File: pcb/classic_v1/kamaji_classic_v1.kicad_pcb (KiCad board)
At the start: 2 copper layers, 100 x 100 mm, 27 parts, among them J1 USB_A, J2 USB_B, J4 ISP, J5 RJ10, J6 RJ10, J7 RJ10, J8 RJ10, J9 RJ10, Q1 BS170, SW1 SW_Push, SW2 SW_Push, SW3 SW_Push, U1 ATmega328P

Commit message: Classic: Finish first pass of routing
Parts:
- added REF**: MountingHole_3.2mm_M3, MountingHole:MountingHole_3.2mm_M3, F.Cu at (146.5, 53.5)
- added REF**: MountingHole_3.2mm_M3, MountingHole:MountingHole_3.2mm_M3, F.Cu at (53.5, 53.5)
- added REF**: MountingHole_3.2mm_M3, MountingHole:MountingHole_3.2mm_M3, F.Cu at (53.5, 146.5)
- added REF**: MountingHole_3.2mm_M3, MountingHole:MountingHole_3.2mm_M3, F.Cu at (146.5, 146.5)
- J5: value RJ10 -> P1
- J6: value RJ10 -> P2
- J7: value RJ10 -> P3
- J8: value RJ10 -> P4
- J9: value RJ10 -> P5
- U1: value ATmega328P -> ATmega328P-P
- moved R1 7.10 mm to (145.5, 75.9)
- moved J4 2.66 mm to (88.5, 136.5)
- moved R2 2.57 mm to (83.4, 121.3)
- moved BZ1 2.00 mm to (113.4, 140.0)
- moved C1 1.38 mm to (101.9, 102.9)
- moved C2 1.38 mm to (99.2, 116.4)
- moved U1 1.38 mm to (117.0, 105.9)
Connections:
- SW3 pad 1: /CBTN2 -> /CBTN3
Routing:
- net VCC: track 0.00 -> 286.6 mm
- net /CBTN3: track 0.00 -> 88.0 mm, vias 0 -> 2
- net /LCD_RS: track 0.00 -> 74.5 mm, vias 0 -> 1
- net /LCD_EN: track 0.00 -> 71.0 mm, vias 0 -> 1
- net /RESET: track 0.00 -> 67.7 mm, vias 0 -> 1
- net /PLED5: track 0.00 -> 67.4 mm
- net /PLED1: track 0.00 -> 64.5 mm, vias 0 -> 1
- net /PBTN1: track 0.00 -> 63.7 mm, vias 0 -> 1
- net /PBTN5: track 0.00 -> 59.5 mm
- net /PLED3: track 0.00 -> 57.6 mm, vias 0 -> 1
- net /PBTN3: track 0.00 -> 56.9 mm, vias 0 -> 1
- net /PBTN4: track 0.00 -> 54.5 mm, vias 0 -> 1
- net /LCD_D2: track 0.00 -> 53.9 mm
- net /LCD_D1: track 0.00 -> 53.9 mm
- net /LCD_D3: track 0.00 -> 53.9 mm
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- added copper zone on B.Cu, net GND
- added copper zone on F.Cu, net GND
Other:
- outline, holes or cut-outs redrawn

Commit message: Final PCB layout tweaks
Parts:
- DS1: value WC1602A -> LCD 1602
- moved R8 12.0 mm to (54.3, 61.0), turned to 0 degrees
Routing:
- net Net-(J9-Pad2): track 10.1 -> 17.0 mm
- net /PLED5: track 67.4 -> 64.1 mm
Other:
- board text added: "Kamaji Classic v1.0 github.com/iley/kamaji"
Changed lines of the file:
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@@
       (viasonmask false)
       (mode 1)
-      (useauxorigin false)
+      (useauxorigin true)
       (hpglpennumber 1)
       (hpglpenspeed 20)
@@
       (plotinvisibletext false)
       (sketchpadsonfab false)
-      (subtractmaskfromsilk false)
+      (subtractmaskfromsilk true)
       (outputformat 1)
       (mirror false)
-      (drillshape 1)
+      (drillshape 0)
       (scaleselection 1)
-      (outputdirectory "")
+      (outputdirectory "gerbers/")
     )
   )
@@
         (effects (font (size 1 1) (thickness 0.15)))
     )
-    (fp_text value "Contrast" (at -4.96 -2.54 -180) (layer "F.SilkS")
+    (fp_text value "Contrast" (at 5.04 -2.54 -180) (layer "F.SilkS")
         (effects (font (size 1 1) (thickness 0.15)))
     )
@@
     (fp_line (start 13.28 15.26) (end 4.38 15.26)
       (stroke (width 0.1) (type solid)) (layer "F.Fab"))
-    (pad "1" thru_hole roundrect (at 0 0 270) (size 1.7 1.7) (drill 1) (layers "*.Cu" "*.Mask") (roundrect_rratio 0.147059)
+    (pad "1" thru_hole roundrect (at 0 0 270) (size 1.7 1.7) (drill 1) (layers "*.Cu" "*.Mask") (roundrect_rratio 0.1470588235)
       (net 21 "/CBTN2") (pinfunction "Pin_1") (pintype "passive"))
     (pad "2" thru_hole circle (at 2.54 0 270) (size 1.7 1.7) (drill 1) (layers "*.Cu" "*.Mask")
@@
   )
   (footprint "Resistor_THT:R_Axial_DIN0207_L6.3mm_D2.5mm_P10.16mm_Horizontal" (layer "F.Cu")
-    (at 61.5 51.34 -90)
+    (at 54.34 61)
     (descr "Resistor, Axial_DIN0207 series, Axial, Horizontal, pin pitch=10.16mm, 0.25W = 1/4W, length*diameter=6.3*2.5mm^2, http://cdn-reichelt.de/documents/datenblatt/B400/1_4W%23YAG.pdf")
     (tags "Resistor Axial_DIN0207 series Axial Horizontal pin pitch 10.16mm 0.25W = 1/4W length 6.3mm diameter 2.5mm")
@@
     (property "ki_keywords" "R res resistor")
     (attr through_hole)
-    (fp_text reference "R8" (at 5.08 -2.37 90) (layer "F.SilkS") hide
-        (effects (font (size 1 1) (thickness 0.15)))
-    )
-    (fp_text value "1K" (at 5.16 0 90) (layer "F.SilkS")
-        (effects (font (size 1 1) (thickness 0.15)))
-    )
-    (fp_text user "${REFERENCE}" (at 5.16 2 90) (layer "F.Fab")
+    (fp_text reference "R8" (at 5.08 -2.37) (layer "F.SilkS") hide
+        (effects (font (size 1 1) (thickness 0.15)))
+    )
+    (fp_text value "1K" (at 5.16 0) (layer "F.SilkS")
+        (effects (font (size 1 1) (thickness 0.15)))
+    )
+    (fp_text user "${REFERENCE}" (at 5.16 2) (layer "F.Fab")
         (effects (font (size 1 1) (thickness 0.15)))
     )
@@
     (fp_line (start 10.16 0) (end 8.23 0)
       (stroke (width 0.1) (type solid)) (layer "F.Fab"))
-    (pad "1" thru_hole circle (at 0 0 270) (size 1.6 1.6) (drill 0.8) (layers "*.Cu" "*.Mask")
+    (pad "1" thru_hole circle (at 0 0) (size 1.6 1.6) (drill 0.8) (layers "*.Cu" "*.Mask")
       (net 34 "Net-(J9-Pad2)") (pintype "passive"))
-    (pad "2" thru_hole oval (at 10.16 0 270) (size 1.6 1.6) (drill 0.8) (layers "*.Cu" "*.Mask")
+    (pad "2" thru_hole oval (at 10.16 0) (size 1.6 1.6) (drill 0.8) (layers "*.Cu" "*.Mask")
       (net 41 "/PLED5") (pintype "passive"))
     (model "${KICAD6_3DMODEL_DIR}/Resistor_THT.3dshapes/R_Axial_DIN0207_L6.3mm_D2.5mm_P10.16mm_Horizontal.wrl"
@@
         (effects (font (size 1 1) (thickness 0.15)))
     )
-    (fp_text value "WC1602A" (at 0.49948 4.5007 180) (layer "F.SilkS")
+    (fp_text value "LCD 1602" (at 0.49948 4.5007 180) (layer "F.SilkS")
         (effects (font (size 1 1) (thickness 0.15)))
     )
@@
     (fp_arc (start 63.7 8) (mid 64.053553 8.146447) (end 64.2 8.5)
       (stroke (width 0.12) (type solid)) (layer "F.SilkS"))
-    (fp_arc (start 64.20104 22.49932) (mid 64.054479 22.85315) (end 63.70066 22.9997)
+    (fp_arc (start 64.20104 22.49932) (mid 64.054473 22.853115) (end 63.70066 22.9997)
       (stroke (width 0.12) (type solid)) (layer "F.SilkS"))
     (fp_line (start -8.25 -2.75) (end -8.25 33.75)
@@
   (gr_line (start 149 150) (end 51 150)
     (stroke (width 0.1) (type default)) (layer "Edge.Cuts"))
+  (gr_text "Kamaji Classic v1.0\ngithub.com/iley/kamaji" (at 100 89) (layer "B.SilkS")
+    (effects (font (size 2 2) (thickness 0.3)) (justify bottom mirror))
+  )
   (segment (start 84.75 133.25) (end 84.75 114.29) (width 0.25) (layer "F.Cu") (net 1))
   (segment (start 84.75 114.29) (end 83.96 113.5) (width 0.25) (layer "F.Cu") (net 1))
@@
   (segment (start 83.428961 131.420012) (end 83.428961 136.451039) (width 0.25) (layer "F.Cu") (net 23))
   (segment (start 119.75 108.65) (end 116.98 105.88) (width 0.25) (layer "F.Cu") (net 23))
-  (segment (start 119.75 130.75) (end 119.75 108.65) (width 0.25) (layer "F.Cu") (net 23))
-  (segment (start 119 131.5) (end 119.75 130.75) (width 0.25) (layer "F.Cu") (net 23))
-  (via (at 119 131.5) (size 0.8) (drill 0.4) (layers "F.Cu" "B.Cu") (net 23))
-  (segment (start 83.428961 131.420012) (end 118.920012 131.420012) (width 0.25) (layer "B.Cu") (net 23))
-  (segment (start 118.920012 131.420012) (end 119 131.5) (width 0.25) (layer "B.Cu") (net 23))
+  (segment (start 119.75 131.5) (end 119.75 108.65) (width 0.25) (layer "F.Cu") (net 23))
+  (via (at 119.75 131.5) (size 0.8) (drill 0.4) (layers "F.Cu" "B.Cu") (net 23))
+  (segment (start 119.670012 131.420012) (end 83.428961 131.420012) (width 0.25) (layer "B.Cu") (net 23))
+  (segment (start 119.75 131.5) (end 119.670012 131.420012) (width 0.25) (layer "B.Cu") (net 23))
   (segment (start 95.949 135.051) (end 95.75 135.25) (width 0.25) (layer "F.Cu") (net 24))
   (segment (start 95.949 115.329) (end 95.949 135.051) (width 0.25) (layer "F.Cu") (net 24))
@@
   (segment (start 87.5 102.75) (end 90.99 102.75) (width 0.25) (layer "B.Cu") (net 33))
   (segment (start 90.99 102.75) (end 94.12 105.88) (width 0.25) (layer "B.Cu") (net 33))
-  (segment (start 66.7 56.54) (end 69.49 56.54) (width 0.25) (layer "F.Cu") (net 34))
-  (segment (start 61.5 51.34) (end 66.7 56.54) (width 0.25) (layer "F.Cu") (net 34))
+  (segment (start 58.8 56.54) (end 69.49 56.54) (width 0.25) (layer "F.Cu") (net 34))
+  (segment (start 54.34 61) (end 58.8 56.54) (width 0.25) (layer "F.Cu") (net 34))
   (segment (start 72.79 56.54) (end 71.53 56.54) (width 0.25) (layer "F.Cu") (net 35))
   (segment (start 84.96552 65.091888) (end 82.373632 62.5) (width 0.25) (layer "F.Cu") (net 35))
@@
   (segment (start 90.08 104.38) (end 90.08 61) (width 0.25) (layer "F.Cu") (net 40))
   (segment (start 91.58 105.88) (end 90.08 104.38) (width 0.25) (layer "F.Cu") (net 40))
-  (segment (start 80.583632 63.25) (end 78.125 63.25) (width 0.25) (layer "F.Cu") (net 41))
-  (segment (start 78.125 63.25) (end 73.375 58.5) (width 0.25) (layer "F.Cu") (net 41))
-  (segment (start 86.5 105.88) (end 82.42552 101.80552) (width 0.25) (layer "F.Cu") (net 41))
-  (segment (start 82.42552 65.091888) (end 80.583632 63.25) (width 0.25) (layer "F.Cu") (net 41))
-  (segment (start 64.5 58.5) (end 61.5 61.5) (width 0.25) (layer "F.Cu") (net 41))
-  (segment (start 82.42552 101.80552) (end 82.42552 65.091888) (width 0.25) (layer "F.Cu") (net 41))
-  (segment (start 73.375 58.5) (end 64.5 58.5) (width 0.25) (layer "F.Cu") (net 41))
+  (segment (start 74 59) (end 78.5 63.5) (width 0.25) (layer "F.Cu") (net 41))
+  (segment (start 82.51552 64.51552) (end 82.51552 101.89552) (width 0.25) (layer "F.Cu") (net 41))
+  (segment (start 81.5 63.5) (end 82.51552 64.51552) (width 0.25) (layer "F.Cu") (net 41))
+  (segment (start 78.5 63.5) (end 81.5 63.5) (width 0.25) (layer "F.Cu") (net 41))
+  (segment (start 64.5 61) (end 66.5 59) (width 0.25) (layer "F.Cu") (net 41))
+  (segment (start 82.51552 101.89552) (end 86.5 105.88) (width 0.25) (layer "F.Cu") (net 41))
+  (segment (start 66.5 59) (end 74 59) (width 0.25) (layer "F.Cu") (net 41))
   (segment (start 86.5 113.5) (end 86.5 124) (width 0.25) (layer "F.Cu") (net 42))
   (via (at 86.5 124) (size 0.8) (drill 0.4) (layers "F.Cu" "B.Cu") (net 42))

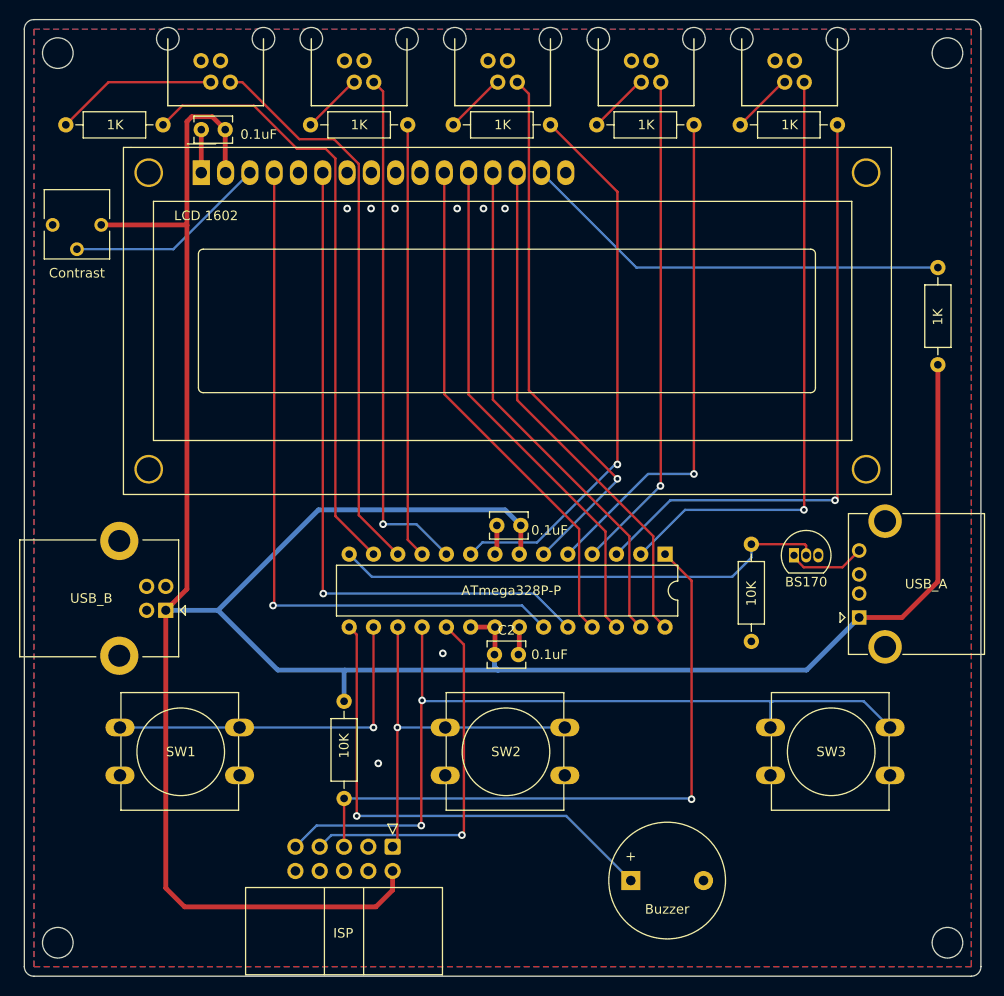
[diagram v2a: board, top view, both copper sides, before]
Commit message: Minor tweaks to the classic PCB
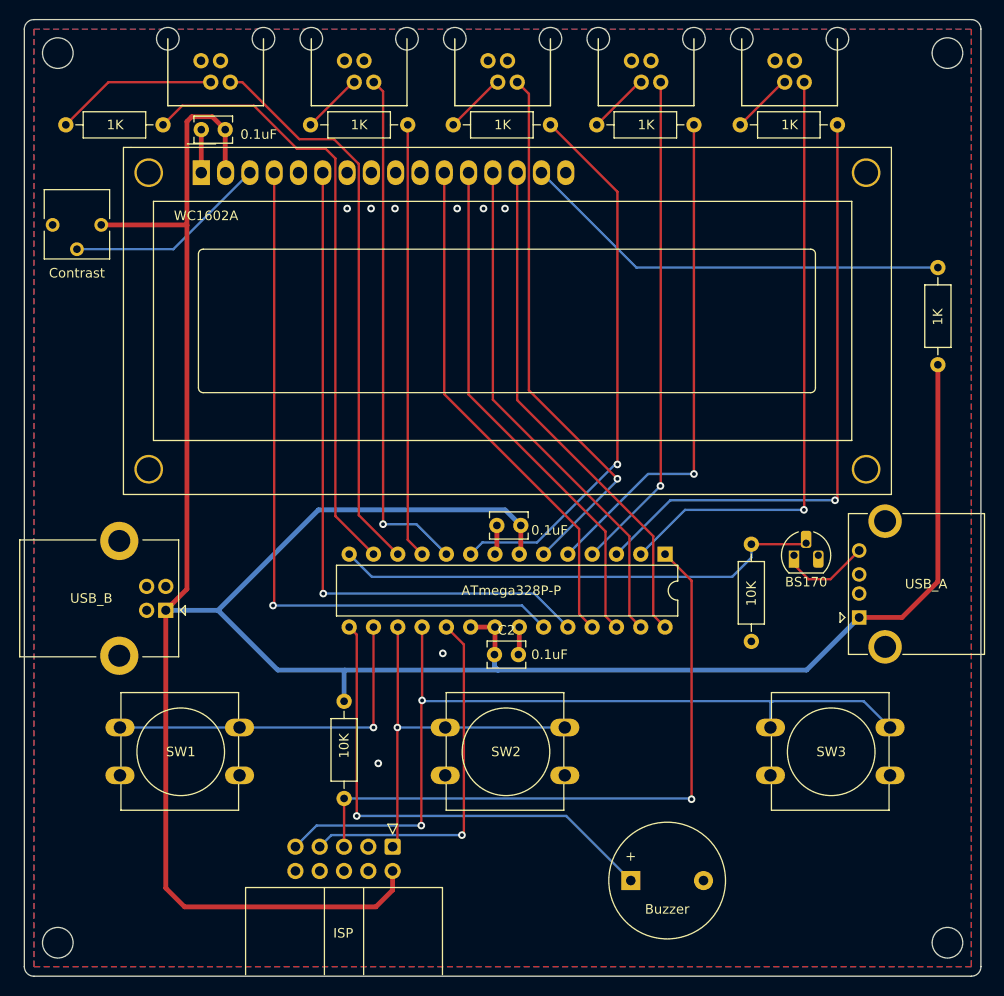
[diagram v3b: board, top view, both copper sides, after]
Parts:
- DS1: value LCD 1602 -> WC1602A
- Q1: footprint Package_TO_SOT_THT:TO-92_Inline -> Package_TO_SOT_THT:TO-92_HandSolder
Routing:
- net Net-(J1-GND): track 8.19 -> 9.66 mm
- net /LAMP: track 52.1 -> 51.0 mm
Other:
- board text added: "Kamaji Classic v1.1 github.com/iley/kamaji"
- board text removed: "Kamaji Classic v1.0 github.com/iley/kamaji"
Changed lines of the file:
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@@
     )
   )
-  (footprint "Package_TO_SOT_THT:TO-92_Inline" (layer "F.Cu")
+  (footprint "Package_TO_SOT_THT:TO-92_HandSolder" (layer "F.Cu")
     (at 130.46 106)
-    (descr "TO-92 leads in-line, narrow, oval pads, drill 0.75mm (see NXP sot054_po.pdf)")
+    (descr "TO-92 leads molded, narrow, drill 0.75mm, handsoldering variant with enlarged pads (see NXP sot054_po.pdf)")
     (tags "to-92 sc-43 sc-43a sot54 PA33 transistor")
     (property "Sheetfile" "kamaji_classic_v1.kicad_sch")
@@
     (property "ki_keywords" "transistor NMOS N-MOS N-MOSFET simulation")
     (attr through_hole)
-    (fp_text reference "Q1" (at 1.27 -3.56) (layer "F.SilkS") hide
+    (fp_text reference "Q1" (at 1.27 -4.4) (layer "F.SilkS") hide
         (effects (font (size 1 1) (thickness 0.15)))
     )
@@
     (fp_line (start -0.53 1.85) (end 3.07 1.85)
       (stroke (width 0.12) (type solid)) (layer "F.SilkS"))
-    (fp_arc (start -0.568478 1.838478) (mid -1.132087 -0.994977) (end 1.27 -2.6)
-      (stroke (width 0.12) (type solid)) (layer "F.SilkS"))
-    (fp_arc (start 1.27 -2.6) (mid 3.672087 -0.994977) (end 3.108478 1.838478)
-      (stroke (width 0.12) (type solid)) (layer "F.SilkS"))
-    (fp_line (start -1.46 -2.73) (end -1.46 2.01)
-      (stroke (width 0.05) (type solid)) (layer "F.CrtYd"))
-    (fp_line (start -1.46 -2.73) (end 4 -2.73)
+    (fp_arc (start -0.541875 1.841741) (mid -1.247231 -0.581764) (end 0.45 -2.45)
+      (stroke (width 0.12) (type solid)) (layer "F.SilkS"))
+    (fp_arc (start 2.05 -2.45) (mid 3.769931 -0.601036) (end 3.078445 1.827684)
+      (stroke (width 0.12) (type solid)) (layer "F.SilkS"))
+    (fp_line (start -1.46 -3.05) (end -1.46 2.01)
+      (stroke (width 0.05) (type solid)) (layer "F.CrtYd"))
+    (fp_line (start -1.46 -3.05) (end 4 -3.05)
       (stroke (width 0.05) (type solid)) (layer "F.CrtYd"))
     (fp_line (start 4 2.01) (end -1.46 2.01)
       (stroke (width 0.05) (type solid)) (layer "F.CrtYd"))
-    (fp_line (start 4 2.01) (end 4 -2.73)
+    (fp_line (start 4 2.01) (end 4 -3.05)
       (stroke (width 0.05) (type solid)) (layer "F.CrtYd"))
     (fp_line (start -0.5 1.75) (end 3 1.75)
@@
     (fp_arc (start 1.27 -2.48) (mid 3.561221 -0.949055) (end 3.023625 1.753625)
       (stroke (width 0.1) (type solid)) (layer "F.Fab"))
-    (pad "1" thru_hole rect (at 0 0) (size 1.05 1.5) (drill 0.75) (layers "*.Cu" "*.Mask")
+    (pad "1" thru_hole rect (at 0 0) (size 1.1 1.8) (drill 0.75 (offset 0 0.4)) (layers "*.Cu" "*.Mask")
       (net 18 "Net-(J1-GND)") (pinfunction "D") (pintype "passive"))
-    (pad "2" thru_hole oval (at 1.27 0) (size 1.05 1.5) (drill 0.75) (layers "*.Cu" "*.Mask")
+    (pad "2" thru_hole roundrect (at 1.27 -1.27) (size 1.1 1.8) (drill 0.75 (offset 0 -0.4)) (layers "*.Cu" "*.Mask") (roundrect_rratio 0.25)
       (net 36 "/LAMP") (pinfunction "G") (pintype "input"))
-    (pad "3" thru_hole oval (at 2.54 0) (size 1.05 1.5) (drill 0.75) (layers "*.Cu" "*.Mask")
+    (pad "3" thru_hole roundrect (at 2.54 0) (size 1.1 1.8) (drill 0.75 (offset 0 0.4)) (layers "*.Cu" "*.Mask") (roundrect_rratio 0.25)
       (net 2 "GND") (pinfunction "S") (pintype "passive"))
-    (model "${KICAD6_3DMODEL_DIR}/Package_TO_SOT_THT.3dshapes/TO-92_Inline.wrl"
+    (model "${KICAD6_3DMODEL_DIR}/Package_TO_SOT_THT.3dshapes/TO-92.wrl"
       (offset (xyz 0 0 0))
       (scale (xyz 1 1 1))
@@
         (effects (font (size 1 1) (thickness 0.15)))
     )
-    (fp_text value "ISP" (at 9.04 5.16 -180) (layer "F.SilkS")
+    (fp_text value "ISP" (at 9.04 5.16) (layer "F.SilkS")
         (effects (font (size 1 1) (thickness 0.15)))
     )
@@
       (stroke (width 0.12) (type solid)) (layer "F.SilkS"))
     (fp_line (start 4.27 15.37) (end 4.27 -5.21)
-      (stroke (width 0.12) (type solid)) (layer "F.SilkS"))
-    (fp_line (start 13.39 -5.21) (end 13.39 15.37)
       (stroke (width 0.12) (type solid)) (layer "F.SilkS"))
     (fp_line (start 13.39 15.37) (end 4.27 15.37)
@@
         (effects (font (size 1 1) (thickness 0.15)))
     )
-    (fp_text value "LCD 1602" (at 0.49948 4.5007 180) (layer "F.SilkS")
+    (fp_text value "WC1602A" (at 0.49948 4.5007 180) (layer "F.SilkS")
         (effects (font (size 1 1) (thickness 0.15)))
     )
@@
   (gr_line (start 149 150) (end 51 150)
     (stroke (width 0.1) (type default)) (layer "Edge.Cuts"))
-  (gr_text "Kamaji Classic v1.0\ngithub.com/iley/kamaji" (at 100 89) (layer "B.SilkS")
+  (gr_text "Kamaji Classic v1.1\ngithub.com/iley/kamaji" (at 100 89) (layer "B.SilkS")
     (effects (font (size 2 2) (thickness 0.3)) (justify bottom mirror))
   )
@@
   (segment (start 113.98122 75.92) (end 145.5 75.92) (width 0.25) (layer "B.Cu") (net 15))
   (segment (start 104.06052 65.9993) (end 113.98122 75.92) (width 0.25) (layer "B.Cu") (net 15))
-  (segment (start 135.5225 107.25) (end 137.2725 105.5) (width 0.25) (layer "F.Cu") (net 18))
-  (segment (start 130.46 106) (end 130.46 106.225) (width 0.25) (layer "F.Cu") (net 18))
-  (segment (start 130.46 106.225) (end 131.485 107.25) (width 0.25) (layer "F.Cu") (net 18))
-  (segment (start 131.485 107.25) (end 135.5225 107.25) (width 0.25) (layer "F.Cu") (net 18))
+  (segment (start 130.46 106) (end 130.46 106.98) (width 0.25) (layer "F.Cu") (net 18))
+  (segment (start 131.98 108.5) (end 134.2725 108.5) (width 0.25) (layer "F.Cu") (net 18))
+  (segment (start 134.2725 108.5) (end 137.2725 105.5) (width 0.25) (layer "F.Cu") (net 18))
+  (segment (start 130.46 106.98) (end 131.98 108.5) (width 0.25) (layer "F.Cu") (net 18))
   (segment (start 89.04 123.96) (end 89 124) (width 0.25) (layer "F.Cu") (net 21))
   (segment (start 89.04 113.5) (end 89.04 123.96) (width 0.25) (layer "F.Cu") (net 21))
@@
   (segment (start 89.04 105.88) (end 84.96552 101.80552) (width 0.25) (layer "F.Cu") (net 35))
   (segment (start 82.373632 62.5) (end 78.75 62.5) (width 0.25) (layer "F.Cu") (net 35))
-  (segment (start 131.57 104.84) (end 126 104.84) (width 0.25) (layer "F.Cu") (net 36))
-  (segment (start 131.73 106) (end 131.73 105) (width 0.25) (layer "F.Cu") (net 36))
-  (segment (start 131.73 105) (end 131.57 104.84) (width 0.25) (layer "F.Cu") (net 36))
+  (segment (start 131.62 104.84) (end 126 104.84) (width 0.25) (layer "F.Cu") (net 36))
+  (segment (start 131.73 104.73) (end 131.62 104.84) (width 0.25) (layer "F.Cu") (net 36))
   (segment (start 83.96 105.88) (end 86.33 108.25) (width 0.25) (layer "B.Cu") (net 36))
   (segment (start 86.33 108.25) (end 124 108.25) (width 0.25) (layer "B.Cu") (net 36))
